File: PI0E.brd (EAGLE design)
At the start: 36 parts, among them IC1 ENC28J60QFN, T1 WE-LAN-10/100/1000-BASE-T,749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, U2 CAT24C32WI-GT3, U3 TLV1117-33CDCY, X1 22-23-2021, X2 22-23-2021

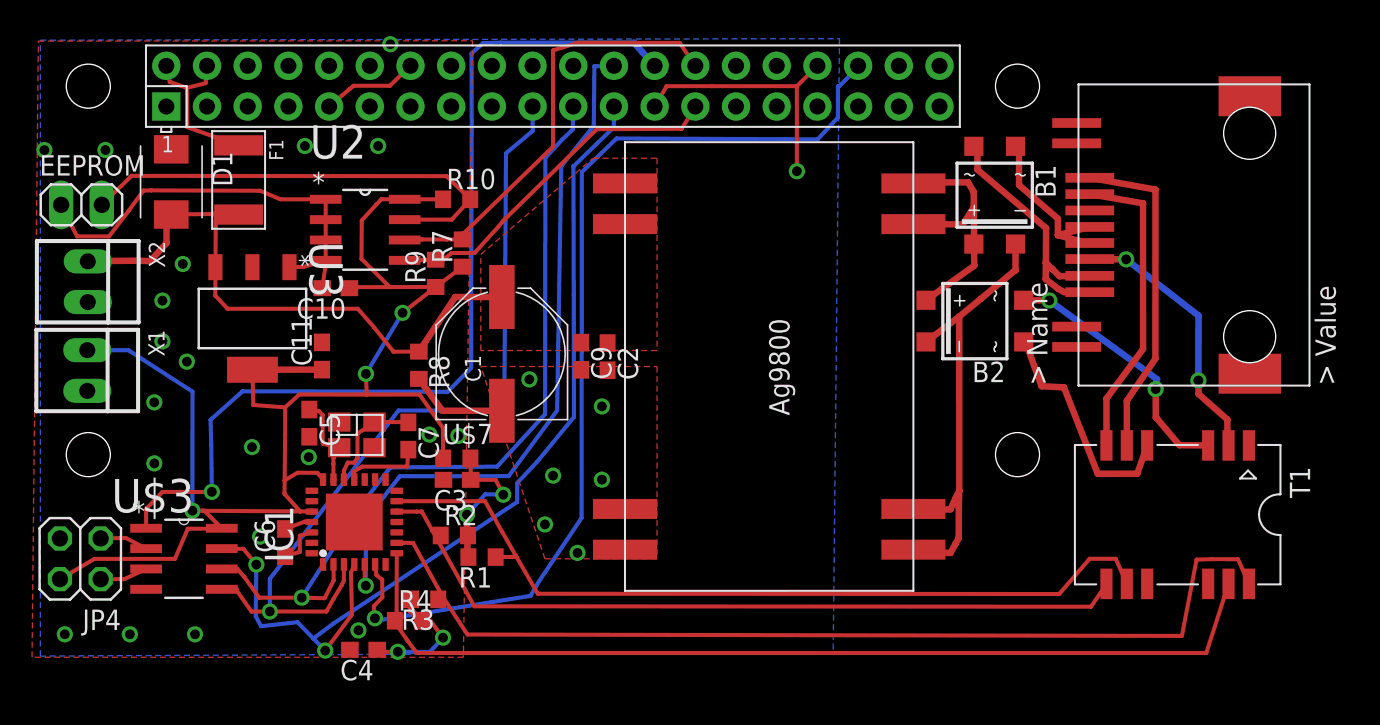
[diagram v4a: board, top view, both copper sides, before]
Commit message: some cleaning of traces
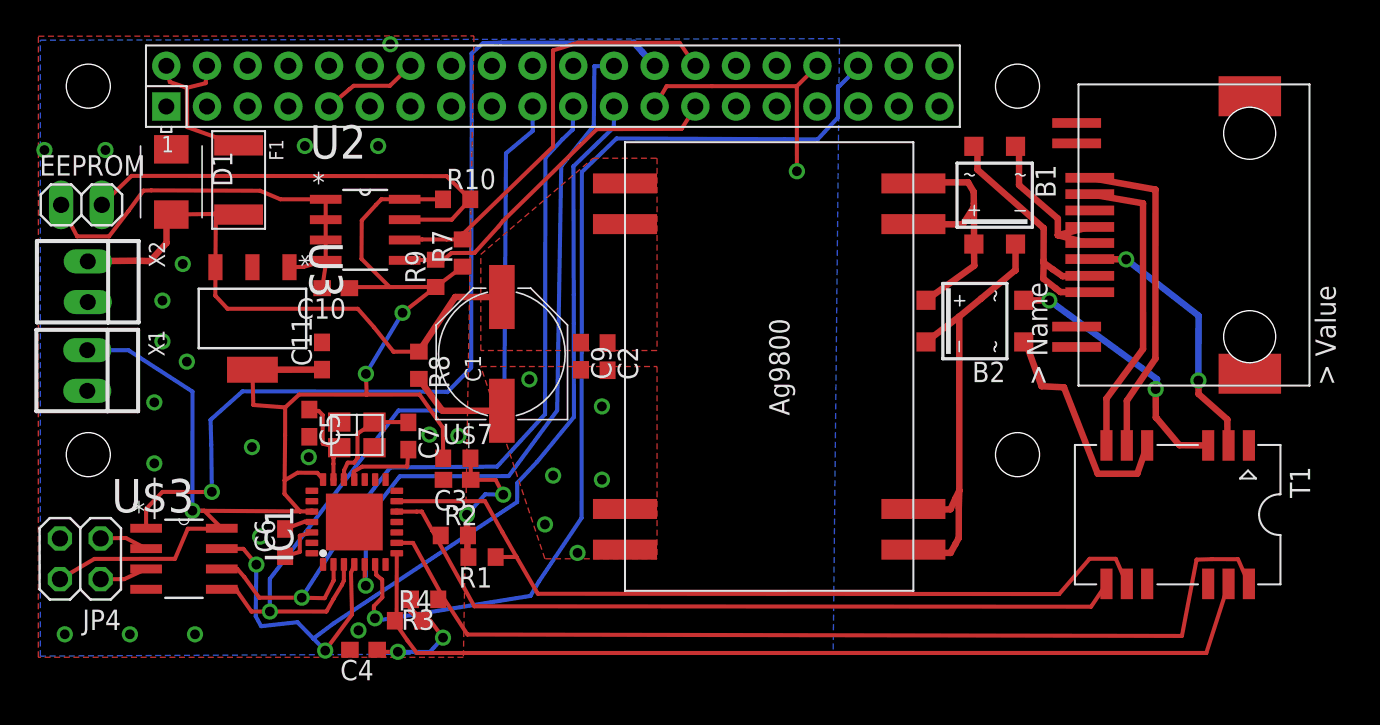
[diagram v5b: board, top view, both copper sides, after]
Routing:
- net GND: vias 26 -> 27
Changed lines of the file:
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@@
 <layer number="25" name="tNames" color="7" fill="1" visible="yes" active="yes"/>
 <layer number="26" name="bNames" color="7" fill="1" visible="yes" active="yes"/>
-<layer number="27" name="tValues" color="7" fill="1" visible="no" active="yes"/>
-<layer number="28" name="bValues" color="7" fill="1" visible="no" active="yes"/>
-<layer number="29" name="tStop" color="7" fill="3" visible="no" active="yes"/>
-<layer number="30" name="bStop" color="7" fill="6" visible="no" active="yes"/>
-<layer number="31" name="tCream" color="7" fill="4" visible="no" active="yes"/>
-<layer number="32" name="bCream" color="7" fill="5" visible="no" active="yes"/>
+<layer number="27" name="tValues" color="7" fill="1" visible="yes" active="yes"/>
+<layer number="28" name="bValues" color="7" fill="1" visible="yes" active="yes"/>
+<layer number="29" name="tStop" color="7" fill="3" visible="yes" active="yes"/>
+<layer number="30" name="bStop" color="7" fill="6" visible="yes" active="yes"/>
+<layer number="31" name="tCream" color="7" fill="4" visible="yes" active="yes"/>
+<layer number="32" name="bCream" color="7" fill="5" visible="yes" active="yes"/>
 <layer number="33" name="tFinish" color="6" fill="3" visible="no" active="yes"/>
 <layer number="34" name="bFinish" color="6" fill="6" visible="no" active="yes"/>
@@
 <wire x1="16.94" y1="25.22" x2="18.3192" y2="25.628" width="0.254" layer="1"/>
 <polygon width="0.4064" layer="1">
-<vertex x="0.384" y="39.313"/>
-<vertex x="27.483" y="39.332"/>
+<vertex x="0.384" y="39.617"/>
+<vertex x="27.57" y="39.636"/>
 <vertex x="26.913" y="0.853"/>
-<vertex x="-0.011" y="0.853"/>
+<vertex x="0.379" y="0.853"/>
 </polygon>
 <polygon width="0.4064" layer="1">
@@
 <via x="17.018" y="32.766" extent="1-16" drill="0.6096" diameter="0.254"/>
 <via x="21.59" y="32.766" extent="1-16" drill="0.6096" diameter="0.254"/>
+<via x="22.352" y="39.116" extent="1-16" drill="0.6096" diameter="0.254"/>
+<wire x1="23.61" y1="37.77" x2="22.352" y2="39.116" width="0" layer="19" extent="1-1"/>
 </signal>
 <signal name="N$5">
@@
 <wire x1="58.776" y1="32.745" x2="59" y2="32.745" width="0.4064" layer="1"/>
 <wire x1="59" y1="32.745" x2="59" y2="31.291" width="0.4064" layer="1"/>
-<wire x1="59" y1="31.291" x2="63.285" y2="27.637" width="0.4064" layer="1"/>
-<wire x1="63.285" y1="27.637" x2="63.275" y2="25.611" width="0.4064" layer="1"/>
-<wire x1="63.269" y1="25.479" x2="63.258" y2="24.455" width="0.4064" layer="1"/>
-<wire x1="63.258" y1="24.455" x2="64.042" y2="23.851" width="0.4064" layer="1"/>
-<wire x1="64.042" y1="23.851" x2="64.4" y2="23.647" width="0.4064" layer="1"/>
-<wire x1="64.4" y1="23.647" x2="66.01" y2="23.626" width="0.4064" layer="1"/>
+<wire x1="59" y1="31.291" x2="63.134" y2="27.637" width="0.4064" layer="1"/>
+<wire x1="63.134" y1="27.637" x2="63.124" y2="25.611" width="0.4064" layer="1"/>
+<wire x1="63.134" y1="25.479" x2="63.105" y2="24.489" width="0.4064" layer="1"/>
+<wire x1="63.105" y1="24.489" x2="63.873" y2="23.885" width="0.4064" layer="1"/>
+<wire x1="63.873" y1="23.885" x2="64.182" y2="23.648" width="0.4064" layer="1"/>
+<wire x1="64.182" y1="23.648" x2="66.01" y2="23.626" width="0.4064" layer="1"/>
 <wire x1="66.01" y1="23.626" x2="66.01" y2="23.641" width="0.4064" layer="1"/>
-<wire x1="66.01" y1="24.661" x2="64.116" y2="24.638" width="0.4064" layer="1"/>
-<wire x1="64.116" y1="24.638" x2="63.691" y2="25.071" width="0.4064" layer="1"/>
-<wire x1="63.691" y1="25.071" x2="63.269" y2="25.479" width="0.4064" layer="1"/>
-<wire x1="63.269" y1="25.479" x2="63.275" y2="25.611" width="0.4064" layer="1"/>
+<wire x1="66.01" y1="24.661" x2="64.318" y2="24.638" width="0.4064" layer="1"/>
+<wire x1="64.318" y1="24.638" x2="63.691" y2="25.071" width="0.4064" layer="1"/>
+<wire x1="63.691" y1="25.071" x2="63.134" y2="25.479" width="0.4064" layer="1"/>
+<wire x1="63.134" y1="25.479" x2="63.124" y2="25.611" width="0.4064" layer="1"/>
 </signal>
 <signal name="N$6">
@@
 <signal name="N$19">
 </signal>
-<signal name="N$35">
-<via x="22.352" y="39.116" extent="1-16" drill="0.6096" diameter="0.254"/>
-</signal>
 <signal name="N$36">

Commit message: copper pour for the 3.3v regulator. A few cleaned traces.
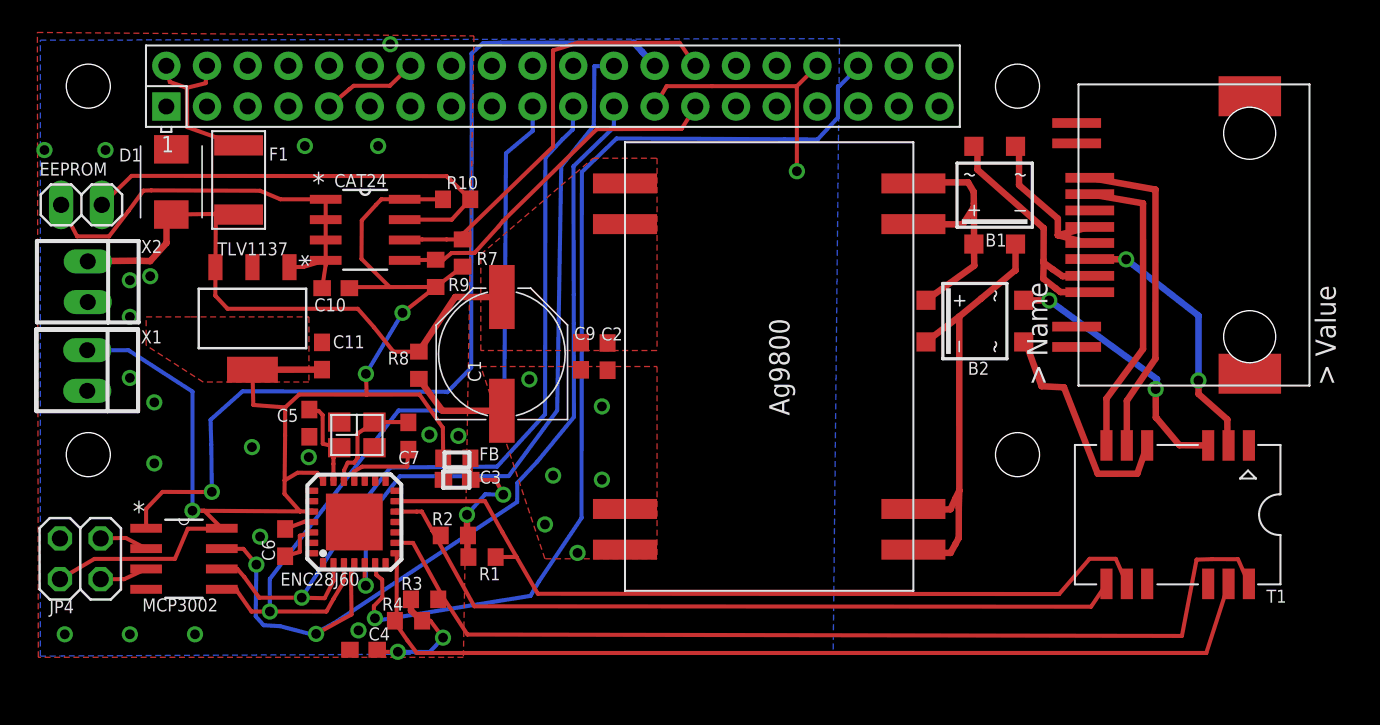
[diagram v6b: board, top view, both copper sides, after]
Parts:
- renumbered IC1 to ENC28J60, U$3 to MCP3002, U$5 to OSC, U$7 to FB, U2 to CAT24, U3 to TLV1137
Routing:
- net SCK: track 59.7 -> 57.9 mm
- added copper zone on layer 1, net +3V3

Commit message: cleared drc issues, cleaned traces
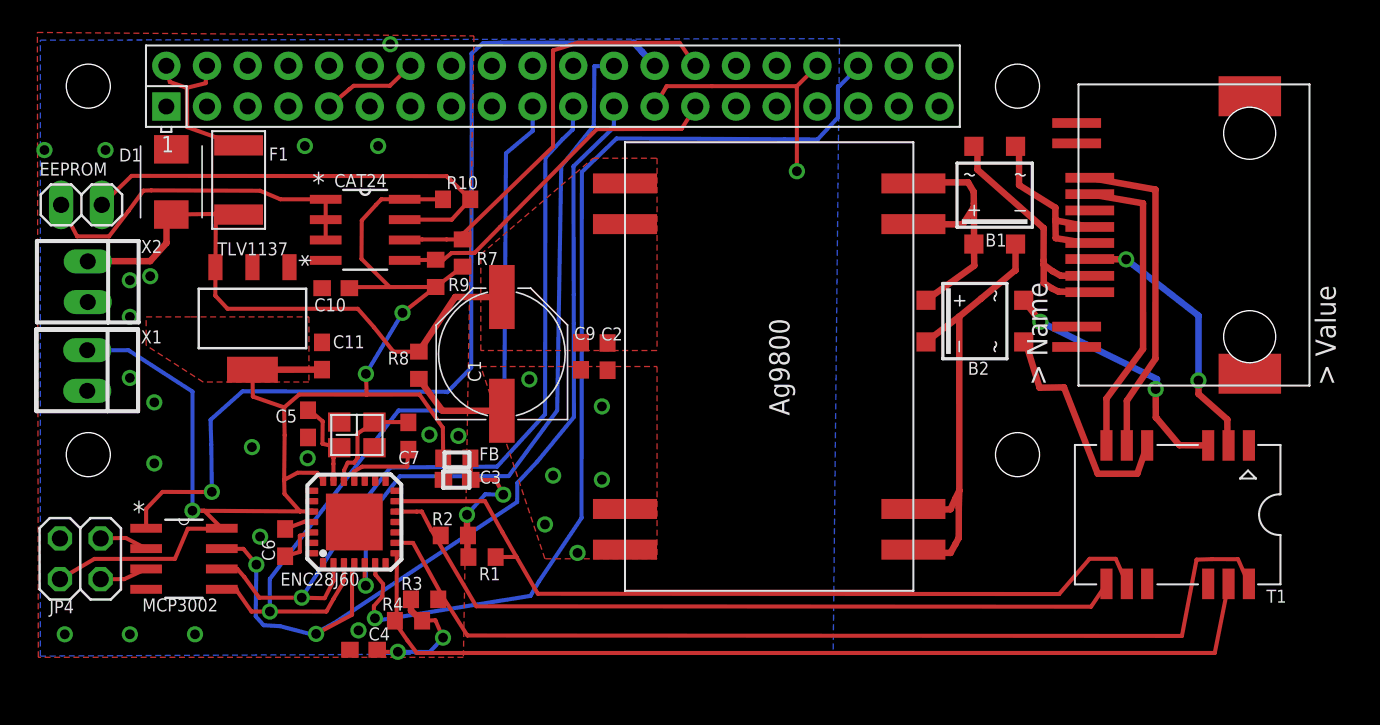
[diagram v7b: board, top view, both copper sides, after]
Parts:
- moved C5 0.09 mm to (17.2, 15.4)
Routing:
- net GND: track 63.9 -> 58.5 mm
- net N$6: track 11.0 -> 11.6 mm
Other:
- board text added: "C Palmer"
